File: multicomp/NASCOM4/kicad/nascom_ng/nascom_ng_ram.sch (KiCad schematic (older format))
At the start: 16 parts, among them U11 74LVC244, U12 74LVC244, U4 AS6C4008-55PCN, U5 AS6C4008-55PCN, U6 74LVC245, U7 74LVC244

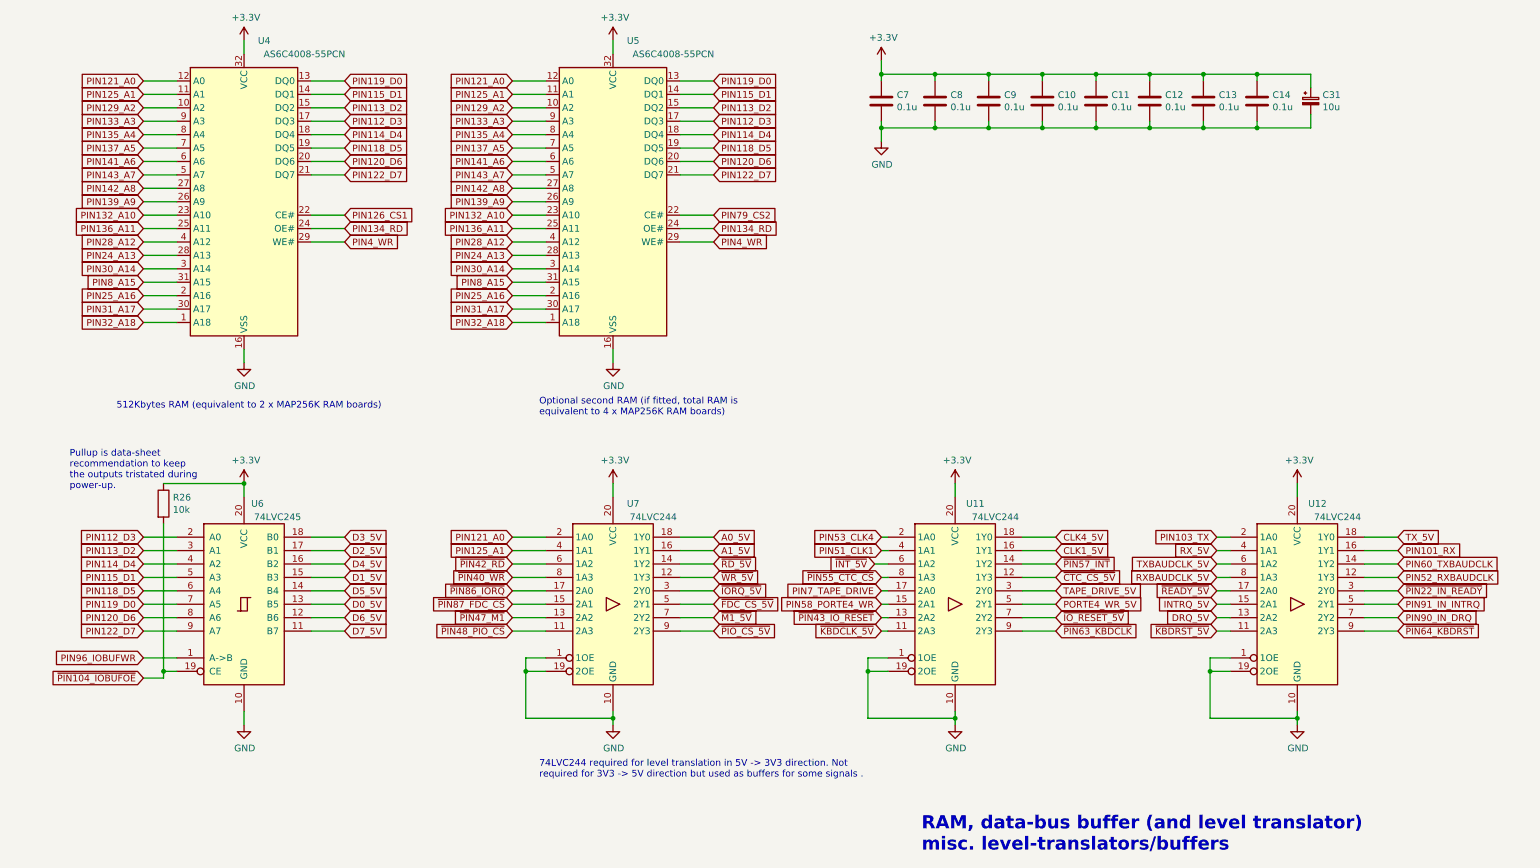
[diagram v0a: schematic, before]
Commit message: All nets routed, ref designators resequenced, nearly finished!
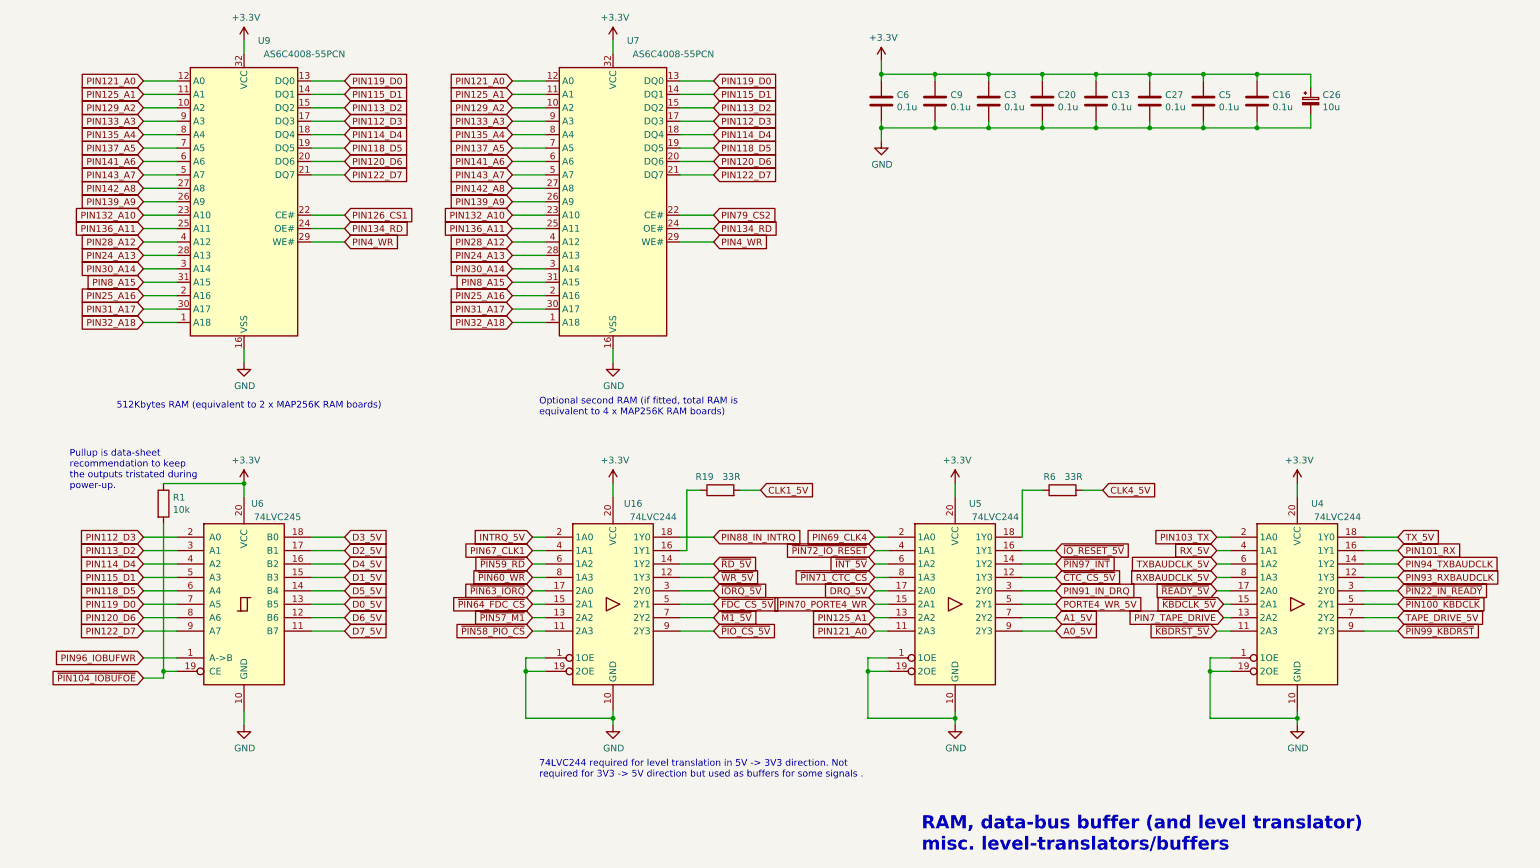
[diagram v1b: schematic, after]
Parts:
- added R19, R6: 33R, Resistor_THT:R_Axial_DIN0204_L3.6mm_D1.6mm_P7.62mm_Horizontal, symbol Device:R
- renumbered C11 to C13, C14 to C16, C10 to C20, C31 to C26, C12 to C27, C9 to C3, C13 to C5, C7 to C6, C8 to C9, R26 to R1, U7 to U16, U12 to U4, U11 to U5, U5 to U7, U4 to U9
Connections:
- net PIN90_IN_DRQ is gone; now on net TAPE_DRIVE_5V: U4.7 (2Y2)
- net ~PIN43_IO_RESET is gone; now on net PIN125_A1: U5.13 (2A2)
- net ~PIN63_KBDCLK is gone; now on net A0_5V: U5.9 (2Y3)
- net A0_5V: no longer U16.18 (1Y0)
- net A1_5V: now also U5.7 (2Y2); no longer U16.16 (1Y1)
- net CLK1_5V: now also R19.2; no longer U5.16 (1Y1)
- net CLK4_5V: now also R6.2; no longer U5.18 (1Y0)
- net DRQ_5V: now also U5.17 (2A0); no longer U4.13 (2A2)
- net INTRQ_5V: now also U16.2 (1A0); no longer U4.15 (2A1)
- net PIN121_A0: now also U5.11 (2A3); no longer U16.2 (1A0)
- net PIN125_A1: no longer U16.4 (1A1)
- net PIN7_TAPE_DRIVE: now also U4.13 (2A2); no longer U5.17 (2A0)
- net TAPE_DRIVE_5V: no longer U5.3 (2Y0)
- net ~IO_RESET_5V: now also U5.16 (1Y1); no longer U5.7 (2Y2)
- net ~KBDCLK_5V: now also U4.15 (2A1); no longer U5.11 (2A3)
- net PIN51_CLK1 renamed ~PIN72_IO_RESET
- net PIN52_RXBAUDCLK renamed PIN93_RXBAUDCLK
- net PIN53_CLK4 renamed PIN69_CLK4
- net PIN58_PORTE4_WR renamed PIN70_PORTE4_WR
- net PIN60_TXBAUDCLK renamed PIN94_TXBAUDCLK
- net PIN91_IN_INTRQ renamed ~PIN100_KBDCLK
- net ~PIN40_WR renamed ~PIN60_WR
- net ~PIN42_RD renamed ~PIN59_RD
- net ~PIN47_M1 renamed ~PIN57_M1
- net ~PIN48_PIO_CS renamed ~PIN58_PIO_CS
- net ~PIN55_CTC_CS renamed ~PIN71_CTC_CS
- net ~PIN57_INT renamed ~PIN97_INT
- net ~PIN64_KBDRST renamed ~PIN99_KBDRST
- net ~PIN86_IORQ renamed ~PIN63_IORQ
- net ~PIN87_FDC_CS renamed ~PIN64_FDC_CS
- new net: R6.1, U5.18 (1Y0)
- new net: R19.1, U16.16 (1Y1)
- new net PIN67_CLK1: U16.4 (1A1)
- new net PIN88_IN_INTRQ: U16.18 (1Y0)
- new net PIN91_IN_DRQ: U5.3 (2Y0)

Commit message: Files for REV A release to PCB manufacture
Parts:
- added C2, C3: 10u, Capacitor_THT:CP_Radial_D5.0mm_P2.50mm, symbol Device:CP_Small
- renumbered C9 to C11, C13 to C17, C16 to C19, C20 to C22, C27 to C30, C26 to C32, C3 to C4, C5 to C6, C6 to C7, R6 to R10, R1 to R5, U6 to U2, U4 to U6
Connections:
- net +3V3: now also C2.1, C3.1
- net A0_5V: now also U5.18 (1Y0); no longer U5.9 (2Y3)
- net GND: now also C2.2, C3.2
- net PIN121_A0: now also U5.2 (1A0); no longer U5.11 (2A3)
- net PIN69_CLK4: now also U5.11 (2A3); no longer U5.2 (1A0)
- net at R10.1: now also U5.9 (2Y3); no longer U5.18 (1Y0)
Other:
- note added: "Near\nSDcard"
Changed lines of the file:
@@
 Optional second RAM (if fitted, total RAM is\nequivalent to 4 x MAP256K RAM boards)
 $Comp
-L 74xx:74LS245 U6
+L 74xx:74LS245 U2
 U 1 1 602F5D56
 P 2050 5100
-F 0 "U6" H 2150 5850 50  0000 C CNN
+F 0 "U2" H 2150 5850 50  0000 C CNN
 F 1 "74LVC245" H 2300 5750 50  0000 C CNN
 F 2 "Package_DIP:DIP-20_W7.62mm" H 2050 5100 50  0001 C CNN
@@
 	4150 5600 4150 5500
 Wire Wire Line
-	7850 5300 8100 5300
-Text GLabel 8100 5300 2    50   Input ~ 0
+	7850 4600 8100 4600
+Text GLabel 8100 4600 2    50   Input ~ 0
 A0_5V
 Wire Wire Line
@@
 PIN125_A1
 Wire Wire Line
-	6850 5300 6750 5300
-Text GLabel 6750 5300 0    50   Input ~ 0
+	6850 4600 6750 4600
+Text GLabel 6750 4600 0    50   Input ~ 0
 PIN121_A0
 Wire Wire Line
@@
 PIN67_CLK1
 Wire Wire Line
-	6850 4600 6750 4600
-Text GLabel 6750 4600 0    50   Input ~ 0
+	6850 5300 6750 5300
+Text GLabel 6750 5300 0    50   Input ~ 0
 PIN69_CLK4
 $Comp
-L 74xx:74HCT244 U4
+L 74xx:74HCT244 U6
 U 1 1 60A1EF8A
 P 9900 5100
-F 0 "U4" H 10050 5850 50  0000 C CNN
+F 0 "U6" H 10050 5850 50  0000 C CNN
 F 1 "74LVC244" H 10200 5750 50  0000 C CNN
 F 2 "Package_DIP:DIP-20_W7.62mm" H 9900 5100 50  0001 C CNN
@@
 P 6800 1350
 AR Path="/62588EF4/6013003B" Ref="C?"  Part="1"
-AR Path="/5FC86EA5/6013003B" Ref="C6"  Part="1"
-F 0 "C6" H 6915 1396 50  0000 L CNN
+AR Path="/5FC86EA5/6013003B" Ref="C7"  Part="1"
+F 0 "C7" H 6915 1396 50  0000 L CNN
 F 1 "0.1u" H 6915 1305 50  0000 L CNN
 F 2 "Capacitor_THT:C_Disc_D3.0mm_W2.0mm_P2.50mm" H 6838 1200 50  0001 C CNN
@@
 P 7200 1350
 AR Path="/62588EF4/60130041" Ref="C?"  Part="1"
-AR Path="/5FC86EA5/60130041" Ref="C9"  Part="1"
-F 0 "C9" H 7315 1396 50  0000 L CNN
+AR Path="/5FC86EA5/60130041" Ref="C11"  Part="1"
+F 0 "C11" H 7315 1396 50  0000 L CNN
 F 1 "0.1u" H 7315 1305 50  0000 L CNN
 F 2 "Capacitor_THT:C_Disc_D3.0mm_W2.0mm_P2.50mm" H 7238 1200 50  0001 C CNN
@@
 P 7600 1350
 AR Path="/62588EF4/60130047" Ref="C?"  Part="1"
-AR Path="/5FC86EA5/60130047" Ref="C3"  Part="1"
-F 0 "C3" H 7715 1396 50  0000 L CNN
+AR Path="/5FC86EA5/60130047" Ref="C4"  Part="1"
+F 0 "C4" H 7715 1396 50  0000 L CNN
 F 1 "0.1u" H 7715 1305 50  0000 L CNN
 F 2 "Capacitor_THT:C_Disc_D3.0mm_W2.0mm_P2.50mm" H 7638 1200 50  0001 C CNN
@@
 P 8000 1350
 AR Path="/62588EF4/6013004D" Ref="C?"  Part="1"
-AR Path="/5FC86EA5/6013004D" Ref="C20"  Part="1"
-F 0 "C20" H 8115 1396 50  0000 L CNN
+AR Path="/5FC86EA5/6013004D" Ref="C22"  Part="1"
+F 0 "C22" H 8115 1396 50  0000 L CNN
 F 1 "0.1u" H 8115 1305 50  0000 L CNN
 F 2 "Capacitor_THT:C_Disc_D3.0mm_W2.0mm_P2.50mm" H 8038 1200 50  0001 C CNN
@@
 P 8400 1350
 AR Path="/62588EF4/60130053" Ref="C?"  Part="1"
-AR Path="/5FC86EA5/60130053" Ref="C13"  Part="1"
-F 0 "C13" H 8515 1396 50  0000 L CNN
+AR Path="/5FC86EA5/60130053" Ref="C17"  Part="1"
+F 0 "C17" H 8515 1396 50  0000 L CNN
 F 1 "0.1u" H 8515 1305 50  0000 L CNN
 F 2 "Capacitor_THT:C_Disc_D3.0mm_W2.0mm_P2.50mm" H 8438 1200 50  0001 C CNN
@@
 P 8800 1350
 AR Path="/62588EF4/60130059" Ref="C?"  Part="1"
-AR Path="/5FC86EA5/60130059" Ref="C27"  Part="1"
-F 0 "C27" H 8915 1396 50  0000 L CNN
+AR Path="/5FC86EA5/60130059" Ref="C30"  Part="1"
+F 0 "C30" H 8915 1396 50  0000 L CNN
 F 1 "0.1u" H 8915 1305 50  0000 L CNN
 F 2 "Capacitor_THT:C_Disc_D3.0mm_W2.0mm_P2.50mm" H 8838 1200 50  0001 C CNN
@@
 P 9200 1350
 AR Path="/62588EF4/6013005F" Ref="C?"  Part="1"
-AR Path="/5FC86EA5/6013005F" Ref="C5"  Part="1"
-F 0 "C5" H 9315 1396 50  0000 L CNN
+AR Path="/5FC86EA5/6013005F" Ref="C6"  Part="1"
+F 0 "C6" H 9315 1396 50  0000 L CNN
 F 1 "0.1u" H 9315 1305 50  0000 L CNN
 F 2 "Capacitor_THT:C_Disc_D3.0mm_W2.0mm_P2.50mm" H 9238 1200 50  0001 C CNN
@@
 P 9600 1350
 AR Path="/62588EF4/60130065" Ref="C?"  Part="1"
-AR Path="/5FC86EA5/60130065" Ref="C16"  Part="1"
-F 0 "C16" H 9715 1396 50  0000 L CNN
+AR Path="/5FC86EA5/60130065" Ref="C19"  Part="1"
+F 0 "C19" H 9715 1396 50  0000 L CNN
 F 1 "0.1u" H 9715 1305 50  0000 L CNN
 F 2 "Capacitor_THT:C_Disc_D3.0mm_W2.0mm_P2.50mm" H 9638 1200 50  0001 C CNN
@@
 $EndComp
 $Comp
-L Device:CP_Small C26
+L Device:CP_Small C32
 U 1 1 6013C2F5
 P 10000 1350
-F 0 "C26" H 10088 1396 50  0000 L CNN
+F 0 "C32" H 10088 1396 50  0000 L CNN
 F 1 "10u" H 10088 1305 50  0000 L CNN
 F 2 "Capacitor_THT:CP_Radial_D5.0mm_P2.50mm" H 10000 1350 50  0001 C CNN
@@
 	5300 5000 5550 5000
 $Comp
-L Device:R R1
+L Device:R R5
 U 1 1 601BB8EF
 P 1450 4350
-F 0 "R1" H 1520 4396 50  0000 L CNN
+F 0 "R5" H 1520 4396 50  0000 L CNN
 F 1 "10k" H 1520 4305 50  0000 L CNN
 F 2 "Resistor_THT:R_Axial_DIN0204_L3.6mm_D1.6mm_P7.62mm_Horizontal" V 1380 4350 50  0001 C CNN
@@
 	9300 4600 9400 4600
 $Comp
-L Device:R R6
+L Device:R R10
 U 1 1 602F32C1
 P 8150 4250
-F 0 "R6" V 8250 4300 50  0000 L CNN
+F 0 "R10" V 8250 4300 50  0000 L CNN
 F 1 "33R" V 8250 4100 50  0000 L CNN
 F 2 "Resistor_THT:R_Axial_DIN0204_L3.6mm_D1.6mm_P7.62mm_Horizontal" V 8080 4250 50  0001 C CNN
@@
 	0    -1   -1   0
 $EndComp
-Wire Wire Line
-	7850 4600 7850 4250
-Wire Wire Line
-	7850 4250 8000 4250
 $Comp
 L Device:R R19
@@
 Wire Wire Line
 	5300 4700 5350 4700
+Text Notes 9950 1750 0    50   ~ 0
+Near\nSDcard
+$Comp
+L Device:CP_Small C3
+U 1 1 60433BB3
+P 10400 1350
+F 0 "C3" H 10488 1396 50  0000 L CNN
+F 1 "10u" H 10488 1305 50  0000 L CNN
+F 2 "Capacitor_THT:CP_Radial_D5.0mm_P2.50mm" H 10400 1350 50  0001 C CNN
+F 3 "~" H 10400 1350 50  0001 C CNN
+	1    10400 1350
+	1    0    0    -1
+$EndComp
+Wire Wire Line
+	10400 1150 10400 1250
+Wire Wire Line
+	10400 1550 10400 1450
+$Comp
+L Device:CP_Small C2
+U 1 1 60440715
+P 10800 1350
+F 0 "C2" H 10888 1396 50  0000 L CNN
+F 1 "10u" H 10888 1305 50  0000 L CNN
+F 2 "Capacitor_THT:CP_Radial_D5.0mm_P2.50mm" H 10800 1350 50  0001 C CNN
+F 3 "~" H 10800 1350 50  0001 C CNN
+	1    10800 1350
+	1    0    0    -1
+$EndComp
+Wire Wire Line
+	10800 1150 10800 1250
+Wire Wire Line
+	10800 1550 10800 1450
+Wire Wire Line
+	10400 1150 10000 1150
+Connection ~ 10000 1150
+Wire Wire Line
+	10400 1550 10000 1550
+Connection ~ 10000 1550
+Wire Wire Line
+	10800 1150 10400 1150
+Connection ~ 10400 1150
+Wire Wire Line
+	10800 1550 10400 1550
+Connection ~ 10400 1550
+Wire Wire Line
+	7900 4250 8000 4250
+Wire Wire Line
+	7850 5300 7900 5300
+Wire Wire Line
+	7900 4250 7900 5300
 $EndSCHEMATC

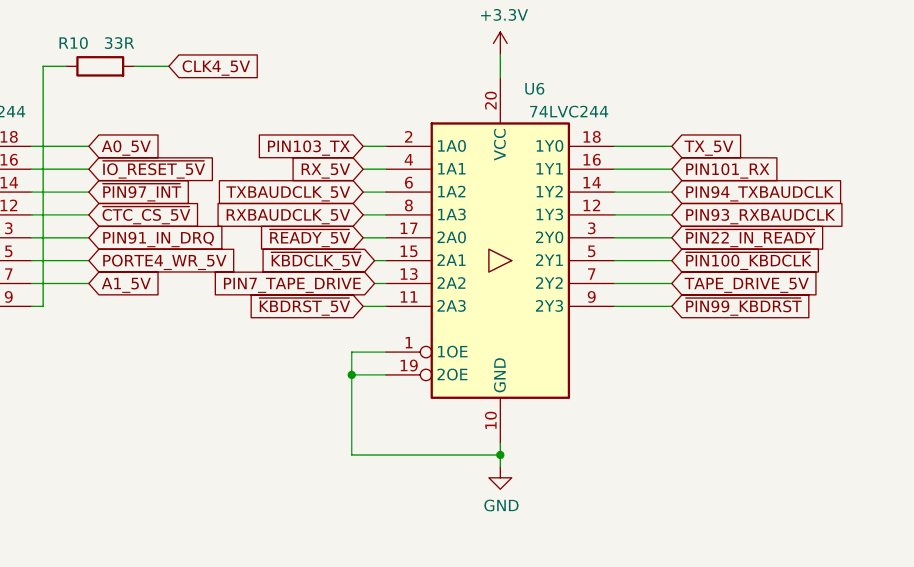
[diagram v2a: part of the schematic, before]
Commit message: Add REVB data-base: schematics, pcb and manufacturing files
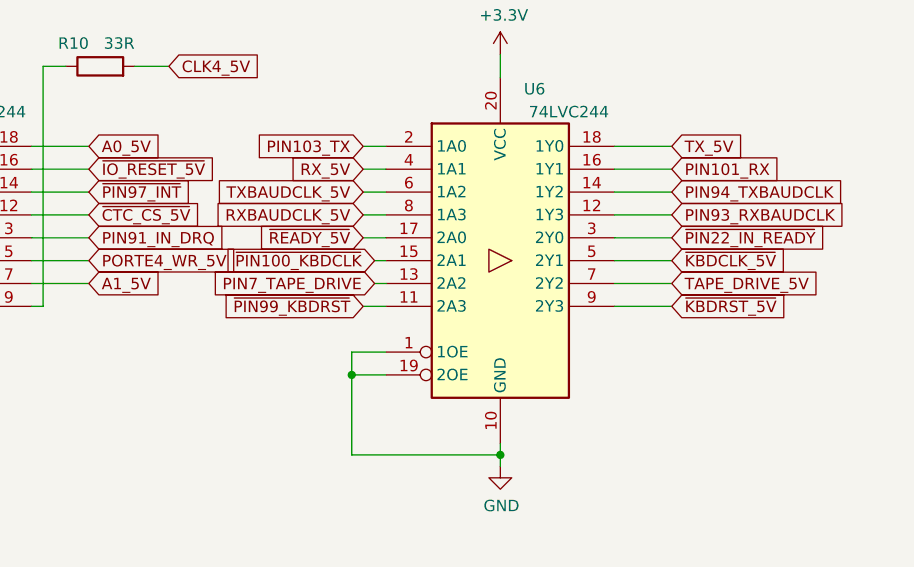
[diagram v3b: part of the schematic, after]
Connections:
- net ~KBDCLK_5V: now also U6.5 (2Y1); no longer U6.15 (2A1)
- net ~KBDRST_5V: now also U6.9 (2Y3); no longer U6.11 (2A3)
- net ~PIN100_KBDCLK: now also U6.15 (2A1); no longer U6.5 (2Y1)
- net ~PIN99_KBDRST: now also U6.11 (2A3); no longer U6.9 (2Y3)
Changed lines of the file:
@@
 Sheet 2 6
 Title "NASCOM 4 - a NASCOM in an FPGA"
-Date ""
-Rev "PRE-A"
+Date "20-Oct-2021"
+Rev "B"
 Comp ""
 Comment1 ""
@@
 Wire Wire Line
 	10400 5300 10650 5300
+Text GLabel 9300 5300 0    50   Input ~ 0
+~PIN99_KBDRST
+Wire Wire Line
+	9400 5300 9300 5300
 Text GLabel 10650 5300 2    50   Input ~ 0
-~PIN99_KBDRST
-Wire Wire Line
-	9400 5300 9300 5300
-Text GLabel 9300 5300 0    50   Input ~ 0
 ~KBDRST_5V
 Wire Wire Line
 	9400 5100 9350 5100
+Text GLabel 10650 5100 2    50   Input ~ 0
+~KBDCLK_5V
+Wire Wire Line
+	10400 5100 10650 5100
 Text GLabel 9350 5100 0    50   Input ~ 0
-~KBDCLK_5V
-Wire Wire Line
-	10400 5100 10650 5100
-Text GLabel 10650 5100 2    50   Input ~ 0
 ~PIN100_KBDCLK
 Wire Wire Line
